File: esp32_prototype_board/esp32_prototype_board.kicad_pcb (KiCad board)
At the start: 4 copper layers, 80 x 60 mm, 0 parts

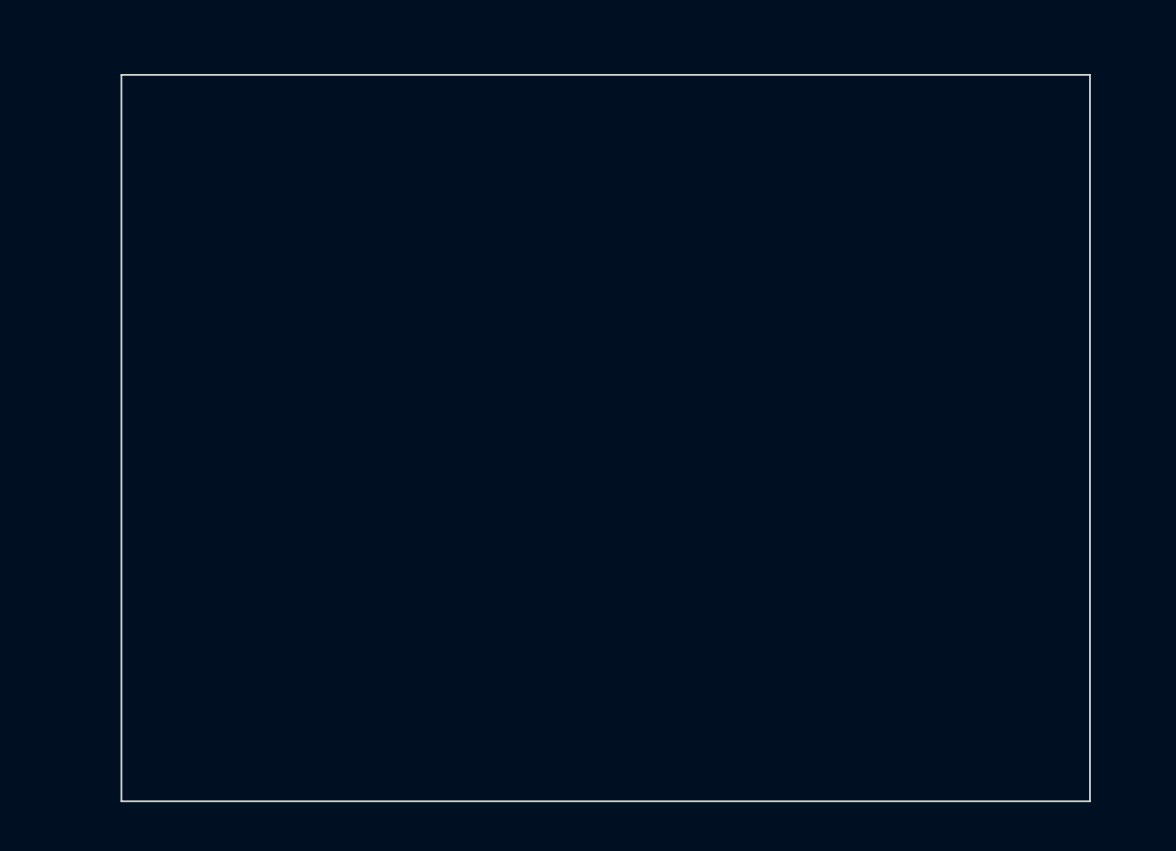
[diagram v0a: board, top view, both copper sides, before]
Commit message: Add initial PCB placement baseline
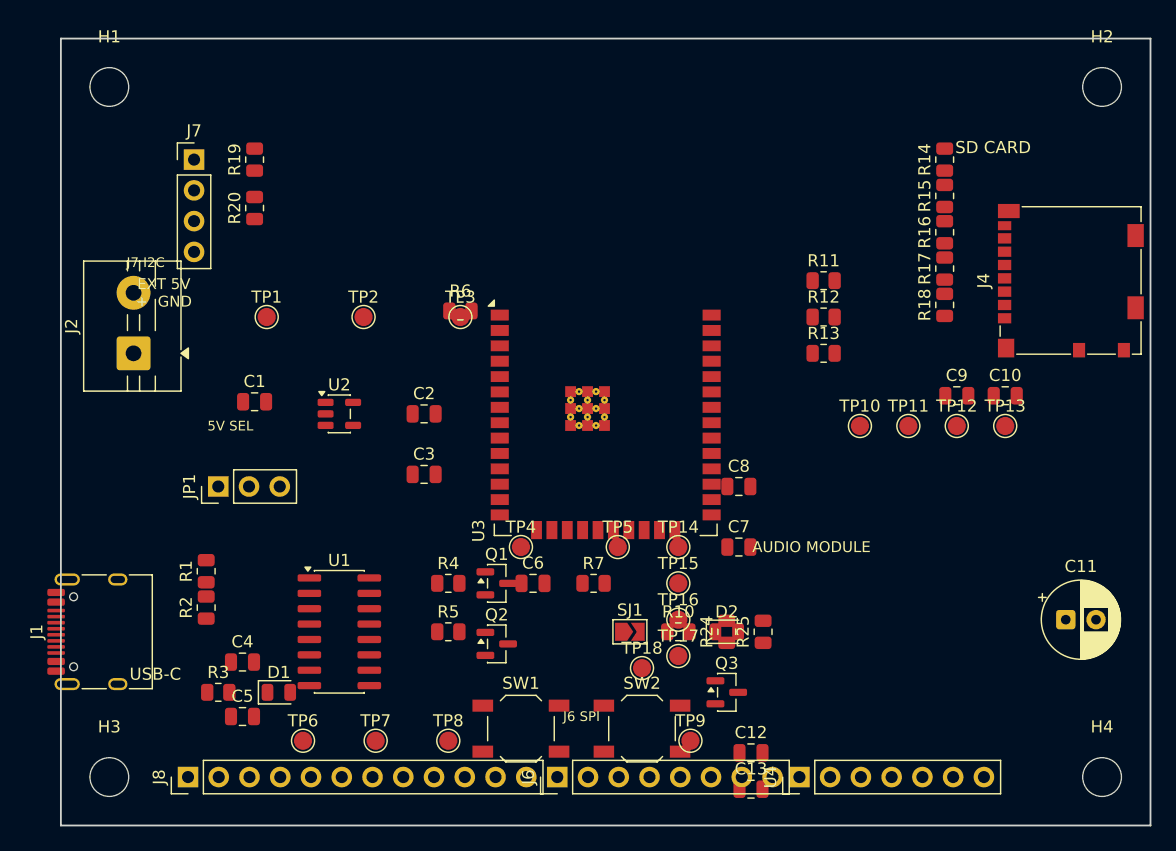
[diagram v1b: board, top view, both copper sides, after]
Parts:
- added C1: 22uF, Capacitor_SMD:C_0805_2012Metric, F.Cu at (66.0, 82.0)
- added C10: 100nF, Capacitor_SMD:C_0805_2012Metric, F.Cu at (128.0, 81.5)
- added C11: 470uF DNP, Capacitor_THT:CP_Radial_D6.3mm_P2.50mm, F.Cu at (133.0, 100.0)
- added C12: 10uF, Capacitor_SMD:C_0805_2012Metric, F.Cu at (107.0, 111.0)
- added C13: 100nF, Capacitor_SMD:C_0805_2012Metric, F.Cu at (107.0, 114.0)
- added C2: 22uF, Capacitor_SMD:C_0805_2012Metric, F.Cu at (80.0, 83.0)
- added C3: 100nF, Capacitor_SMD:C_0805_2012Metric, F.Cu at (80.0, 88.0)
- added C4: 100nF, Capacitor_SMD:C_0805_2012Metric, F.Cu at (65.0, 103.5)
- added C5: 100nF, Capacitor_SMD:C_0805_2012Metric, F.Cu at (65.0, 108.0)
- added C6: 1uF, Capacitor_SMD:C_0805_2012Metric, F.Cu at (89.0, 97.0)
- added C7: 22uF, Capacitor_SMD:C_0805_2012Metric, F.Cu at (106.0, 94.0)
- added C8: 100nF, Capacitor_SMD:C_0805_2012Metric, F.Cu at (106.0, 89.0)
- added C9: 10uF, Capacitor_SMD:C_0805_2012Metric, F.Cu at (124.0, 81.5)
- added D1: 5V PWR, LED_SMD:LED_0805_2012Metric, F.Cu at (68.0, 106.0)
- added D2: STATUS, LED_SMD:LED_0805_2012Metric, F.Cu at (105.0, 101.0)
- added H1: M3, MountingHole:MountingHole_3.2mm_M3, F.Cu at (54.0, 56.0)
- added H2: M3, MountingHole:MountingHole_3.2mm_M3, F.Cu at (136.0, 56.0)
- added H3: M3, MountingHole:MountingHole_3.2mm_M3, F.Cu at (54.0, 113.0)
- added H4: M3, MountingHole:MountingHole_3.2mm_M3, F.Cu at (136.0, 113.0)
- added J1: USB-C USB2 sink, Connector_USB:USB_C_Receptacle_HRO_TYPE-C-31-M-12, F.Cu at (53.6, 101.0)
- added J2: EXT 5V IN, TerminalBlock:TerminalBlock_MaiXu_MX126-5.0-02P_1x02_P5.00mm, F.Cu at (56.0, 78.0)
- added J4: microSD SPI, Connector_Card:microSD_HC_Molex_104031-0811, F.Cu at (133.4, 72.0)
- added J6: SPI EXP, Connector_PinHeader_2.54mm:PinHeader_1x08_P2.54mm_Vertical, F.Cu at (91.0, 113.0)
- added J7: I2C EXP, Connector_PinHeader_2.54mm:PinHeader_1x04_P2.54mm_Vertical, F.Cu at (61.0, 62.0)
- added J8: GPIO EXP, Connector_PinHeader_2.54mm:PinHeader_1x12_P2.54mm_Vertical, F.Cu at (60.5, 113.0)
- added JP1: 5V source select, Connector_PinHeader_2.54mm:PinHeader_1x03_P2.54mm_Vertical, F.Cu at (63.0, 89.0)
- added Q1: SS8050/MMBT3904, Package_TO_SOT_SMD:SOT-23, F.Cu at (86.0, 97.0)
- added Q2: SS8050/MMBT3904, Package_TO_SOT_SMD:SOT-23, F.Cu at (86.0, 102.0)
- added Q3: MMBT3904, Package_TO_SOT_SMD:SOT-23, F.Cu at (105.0, 106.0)
- added R1: 5.1k, Resistor_SMD:R_0805_2012Metric, F.Cu at (62.0, 96.0)
- added R10: 1k, Resistor_SMD:R_0805_2012Metric, F.Cu at (101.0, 101.0)
- added R11: 22R, Resistor_SMD:R_0805_2012Metric, F.Cu at (113.0, 72.0)
- added R12: 22R, Resistor_SMD:R_0805_2012Metric, F.Cu at (113.0, 75.0)
- added R13: 22R, Resistor_SMD:R_0805_2012Metric, F.Cu at (113.0, 78.0)
- added R14: 10k, Resistor_SMD:R_0805_2012Metric, F.Cu at (123.0, 62.0)
- added R15: 10k, Resistor_SMD:R_0805_2012Metric, F.Cu at (123.0, 65.0)
- added R16: 10k, Resistor_SMD:R_0805_2012Metric, F.Cu at (123.0, 68.0)
- added R17: 10k, Resistor_SMD:R_0805_2012Metric, F.Cu at (123.0, 71.0)
- added R18: 10k, Resistor_SMD:R_0805_2012Metric, F.Cu at (123.0, 74.0)
- added R19: 4.7k, Resistor_SMD:R_0805_2012Metric, F.Cu at (66.0, 62.0)
- added R2: 5.1k, Resistor_SMD:R_0805_2012Metric, F.Cu at (62.0, 99.0)
- added R20: 4.7k, Resistor_SMD:R_0805_2012Metric, F.Cu at (66.0, 66.0)
- added R24: 10k, Resistor_SMD:R_0805_2012Metric, F.Cu at (105.0, 101.0)
- added R25: 100k, Resistor_SMD:R_0805_2012Metric, F.Cu at (108.0, 101.0)
- added R3: 2.2k, Resistor_SMD:R_0805_2012Metric, F.Cu at (63.0, 106.0)
- added R4: 10k, Resistor_SMD:R_0805_2012Metric, F.Cu at (82.0, 97.0)
- added R5: 10k, Resistor_SMD:R_0805_2012Metric, F.Cu at (82.0, 101.0)
- added R6: 10k, Resistor_SMD:R_0805_2012Metric, F.Cu at (83.0, 74.5)
- added R7: 10k, Resistor_SMD:R_0805_2012Metric, F.Cu at (94.0, 97.0)
- added SJ1: GPIO2 LED EN, Jumper:SolderJumper-2_P1.3mm_Open_TrianglePad1.0x1.5mm, F.Cu at (97.0, 101.0)
- added SW1: EN/RST, Button_Switch_SMD:SW_SPST_TL3342, F.Cu at (88.0, 109.0)
- added SW2: BOOT, Button_Switch_SMD:SW_SPST_TL3342, F.Cu at (98.0, 109.0)
- added TP1: 5V_SYS, TestPoint:TestPoint_Pad_D1.5mm, F.Cu at (67.0, 75.0)
- added TP10: SD_SCK, TestPoint:TestPoint_Pad_D1.5mm, F.Cu at (116.0, 84.0)
- added TP11: SD_MOSI, TestPoint:TestPoint_Pad_D1.5mm, F.Cu at (120.0, 84.0)
- added TP12: SD_MISO, TestPoint:TestPoint_Pad_D1.5mm, F.Cu at (124.0, 84.0)
- added TP13: SD_CS, TestPoint:TestPoint_Pad_D1.5mm, F.Cu at (128.0, 84.0)
- added TP14: I2S_BCLK, TestPoint:TestPoint_Pad_D1.5mm, F.Cu at (101.0, 94.0)
- added TP15: I2S_WS, TestPoint:TestPoint_Pad_D1.5mm, F.Cu at (101.0, 97.0)
- added TP16: I2S_DOUT, TestPoint:TestPoint_Pad_D1.5mm, F.Cu at (101.0, 100.0)
- added TP17: AMP_MUTE_CTL, TestPoint:TestPoint_Pad_D1.5mm, F.Cu at (101.0, 103.0)
- added TP18: AMP_SD_MODE, TestPoint:TestPoint_Pad_D1.5mm, F.Cu at (98.0, 104.0)
- added TP2: 3V3, TestPoint:TestPoint_Pad_D1.5mm, F.Cu at (75.0, 75.0)
- added TP3: GND, TestPoint:TestPoint_Pad_D1.5mm, F.Cu at (83.0, 75.0)
- added TP4: EN, TestPoint:TestPoint_Pad_D1.5mm, F.Cu at (88.0, 94.0)
- added TP5: BOOT, TestPoint:TestPoint_Pad_D1.5mm, F.Cu at (96.0, 94.0)
- added TP6: UART0_TX, TestPoint:TestPoint_Pad_D1.5mm, F.Cu at (70.0, 110.0)
- added TP7: UART0_RX, TestPoint:TestPoint_Pad_D1.5mm, F.Cu at (76.0, 110.0)
- added TP8: GPIO32, TestPoint:TestPoint_Pad_D1.5mm, F.Cu at (82.0, 110.0)
- added TP9: GPIO33, TestPoint:TestPoint_Pad_D1.5mm, F.Cu at (102.0, 110.0)
- added U1: CH340C, Package_SO:SOIC-16_3.9x9.9mm_P1.27mm, F.Cu at (73.0, 101.0)
- added U2: AP2112K-3.3, Package_TO_SOT_SMD:SOT-23-5, F.Cu at (73.0, 83.0)
- added U3: ESP32-WROOM-32E, RF_Module:ESP32-WROOM-32E, F.Cu at (95.0, 80.1)
- added U4: MAX98357A blue module, Connector_PinHeader_2.54mm:PinHeader_1x07_P2.54mm_Vertical, F.Cu at (111.0, 113.0)
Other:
- board size 80 x 60 mm -> 90 x 65 mm
- board text added: "5V SEL"
- board text added: "AUDIO MODULE"
- board text added: "ESP32 antenna keepout: no copper, traces, parts, screws, or wires"
- board text added: "EXT 5V + GND"
- board text added: "J6 SPI"
- board text added: "J7 I2C"
- board text added: "MAX98357A module body clearance"
- board text added: "Rev A first placement: 90mm x 65mm"
- board text added: "SD CARD"
- board text removed: "5V select 3V3 LDO"
- board text removed: "ESP32 antenna keepout no copper, traces, parts, screws, or wires"
- board text removed: "ESP32-WROOM-32E module body"
- board text removed: "GPIO headers"
- board text removed: "MAX98357A module + speaker"
- board text removed: "Rev A starter outline: 80mm x 60mm"
- board text removed: "microSD socket short SPI traces"

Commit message: adding final PCB files
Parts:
- removed SJ1: GPIO2 LED EN, Jumper:SolderJumper-2_P1.3mm_Open_TrianglePad1.0x1.5mm
- added C14: 100nF, Capacitor_SMD:C_0805_2012Metric, F.Cu at (61.5, 72.0)
- added JP2: GPIO2 LED SW, SweetYaar:SW-SMD_MS-22D28-G020, F.Cu at (77.7, 89.0)
- H1, H2, H3, H4: value M3 -> M3 mounting hole
- JP1: value 5V source select -> 5V source switch; footprint Connector_PinHeader_2.54mm:PinHeader_1x03_P2.54mm_Vertical -> SweetYaar:SW-SMD_MS-22D28-G020
- moved SW2 57.6 mm to (72.6, 57.3)
- moved SW1 57.2 mm to (63.5, 57.3)
- moved R19 44.2 mm to (59.8, 105.8), turned to 0 degrees
- moved C7 42.1 mm to (75.7, 64.8)
- moved C8 40.2 mm to (75.7, 62.6)
- moved R20 39.9 mm to (63.5, 105.8), turned to 180 degrees
- moved J7 39.6 mm to (52.5, 100.6), turned to 90 degrees
- moved R3 35.2 mm to (77.5, 73.9)
- moved C13 33.9 mm to (109.2, 80.2), turned to -90 degrees
- moved D2 32.6 mm to (77.5, 83.5)
- moved C10 31.9 mm to (106.7, 57.8), turned to -90 degrees
- moved D1 31.4 mm to (77.5, 76.1)
- moved C5 30.8 mm to (70.6, 77.7), turned to -90 degrees
- moved C12 30.8 mm to (107.0, 80.2), turned to -90 degrees
- moved C9 30.7 mm to (104.4, 57.8), turned to -90 degrees
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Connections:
- J1 pad A8: (no net) -> unconnected-(J1-SBU1-PadA8)
- J1 pad B8: (no net) -> unconnected-(J1-SBU2-PadB8)
- U1 pad 10: (no net) -> unconnected-(U1-DSR-Pad10)
- U1 pad 11: (no net) -> unconnected-(U1-RI-Pad11)
- U1 pad 12: (no net) -> unconnected-(U1-DCD-Pad12)
- U1 pad 7: (no net) -> unconnected-(U1-NC-Pad7)
- U1 pad 8: (no net) -> unconnected-(U1-NC-Pad8)
- U1 pad 9: (no net) -> unconnected-(U1-CTS-Pad9)
- U2 pad 4: (no net) -> unconnected-(U2-NC-Pad4)
- U3 pad 14: (no net) -> unconnected-(U3-GPIO12-Pad14)
- U3 pad 17: (no net) -> unconnected-(U3-NC/SD2-Pad17)
- U3 pad 18: (no net) -> unconnected-(U3-NC/SD3-Pad18)
- U3 pad 19: (no net) -> unconnected-(U3-NC/CMD-Pad19)
- U3 pad 20: (no net) -> unconnected-(U3-NC/CLK-Pad20)
- U3 pad 21: (no net) -> unconnected-(U3-NC/SD0-Pad21)
- U3 pad 22: (no net) -> unconnected-(U3-NC/SD1-Pad22)
- U3 pad 32: (no net) -> unconnected-(U3-NC-Pad32)
- U4 pad 4: (no net) -> unconnected-(U4-GAIN-Pad4)
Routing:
- net /3V3: track 0.00 -> 212.8 mm, vias 0 -> 10
- net /5V_SYS: track 0.00 -> 182.9 mm, vias 0 -> 8
- net /GND: track 0.00 -> 98.0 mm, vias 0 -> 29
- net /BOOT: track 0.00 -> 93.0 mm, vias 0 -> 2
- net /I2C_SDA: track 0.00 -> 71.9 mm, vias 0 -> 2
- net /I2C_SCL: track 0.00 -> 71.3 mm, vias 0 -> 2
- net /EN: track 0.00 -> 69.7 mm, vias 0 -> 5
- net /SD_MISO: track 0.00 -> 67.2 mm, vias 0 -> 2
- net /UART0_RX: track 0.00 -> 63.8 mm, vias 0 -> 2
- net /UART0_TX: track 0.00 -> 61.0 mm, vias 0 -> 2
- net /GPIO32: track 0.00 -> 60.4 mm, vias 0 -> 5
- net /SD_SCK: track 0.00 -> 56.9 mm, vias 0 -> 1
- net /GPIO33: track 0.00 -> 56.0 mm, vias 0 -> 3
- net /GPIO36: track 0.00 -> 54.0 mm, vias 0 -> 3
- net /I2S_WS: track 0.00 -> 52.7 mm, vias 0 -> 2
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- added copper zone on In1.Cu, net /GND
- added copper zone on In2.Cu, net /GND
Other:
- board size 90 x 65 mm -> 70 x 60 mm
- board text added: "0"
- board text added: "1/TX"
- board text added: "12"
- board text added: "13"
- board text added: "14"
- board text added: "15"
- board text added: "16"
- board text added: "17"
- board text added: "18"
- board text added: "19"
- board text added: "2"
- board text added: "21"
- board text added: "22"
- board text added: "23"
- board text added: "25"
- board text added: "26"
- board text added: "27"
- board text added: "3.3V"
- board text added: "3/RX"
- board text added: "32"
- board text added: "33"
- board text added: "34"
- board text added: "35"
- board text added: "36"
- board text added: "39"
- board text added: "3V3"
- board text added: "4"
- board text added: "5"
- board text added: "5V"
- board text added: "AUDIO MODULE MAX98357A"
- board text added: "BCLK"
- board text added: "BOOT"
- board text added: "CS1"
- board text added: "CS2"
- board text added: "DOUT"
- board text added: "EN"
- board text added: "ESP32 Dev Board (by Zach Moshe)"
- board text added: "EXT"
- board text added: "GND"
- board text added: "GPIO EXPANSION"
- board text added: "I2C"
- board text added: "LED2"
- board text added: "MISO"
- board text added: "MOSI"
- board text added: "MUTE_CTL"
- board text added: "OFF"
- board text added: "ON"
- board text added: "RST/EN"
- board text added: "RX"
- board text added: "Rev A first placement: 70mm x 60mm"
- board text added: "SCK"
- board text added: "SCL"
- board text added: "SD"
- board text added: "SDA"
- board text added: "SD_CS"
- board text added: "SPI"
- board text added: "TX"
- board text added: "USB"
- board text added: "WS"
- board text removed: "AUDIO MODULE"
- board text removed: "ESP32 antenna keepout: no copper, traces, parts, screws, or wires"
- board text removed: "EXT 5V + GND"
- board text removed: "J6 SPI"
- board text removed: "J7 I2C"
- board text removed: "Rev A first placement: 90mm x 65mm"
- board text removed: "SD CARD"
